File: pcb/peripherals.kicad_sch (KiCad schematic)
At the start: 1 part, among them U4 NRF24L01_Breakout

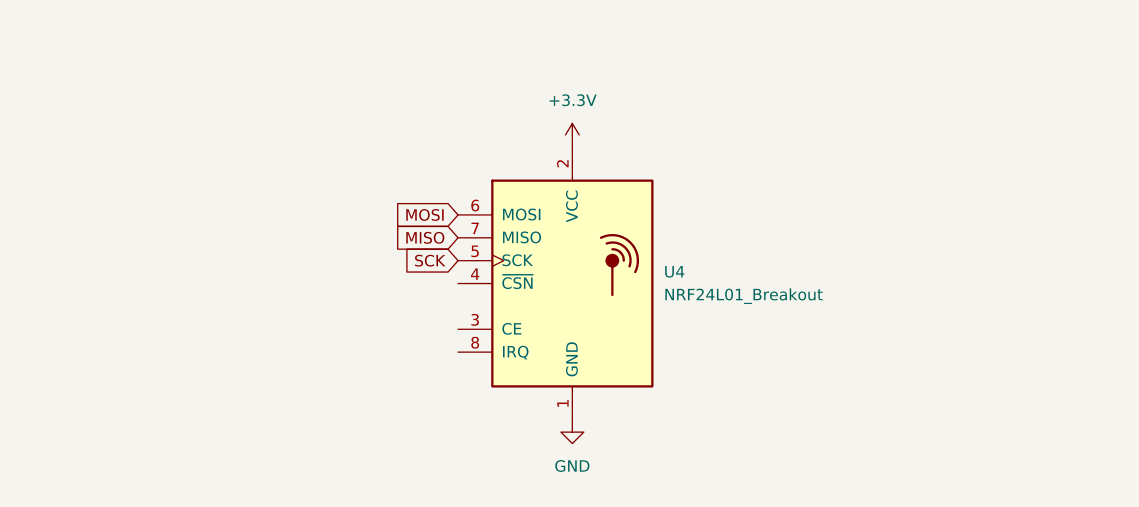
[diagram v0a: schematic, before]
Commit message: [pcb] motor controllers, label/group cleanup
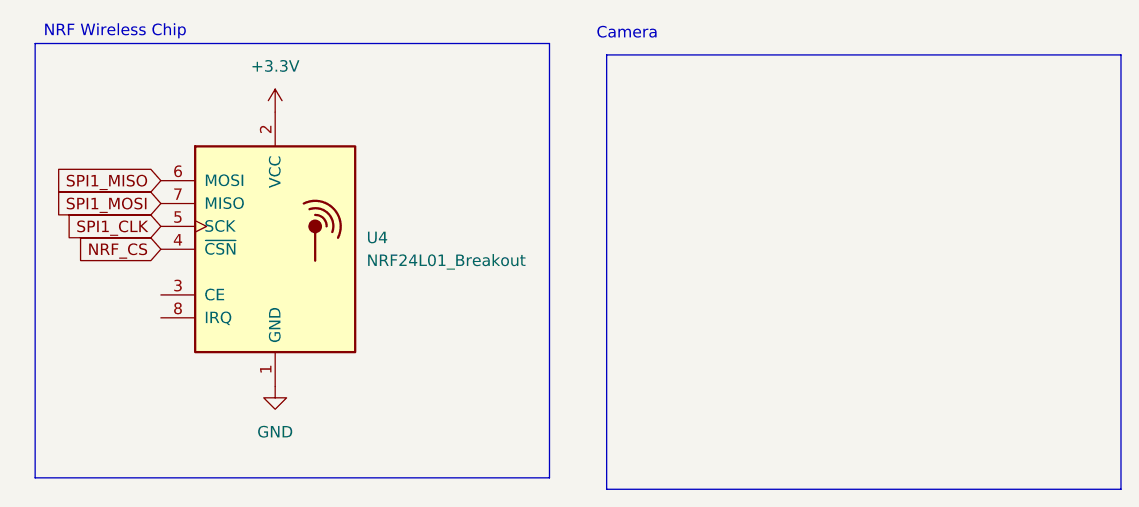
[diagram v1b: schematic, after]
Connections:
- net NRF_CS: now reaches U4.4 (~{CSN})
- net MISO renamed SPI1_MOSI
- net MOSI renamed SPI1_MISO
- net SCK renamed SPI1_CLK
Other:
- note added: "Camera"
- note added: "NRF Wireless Chip"
- moved on the sheet: U4
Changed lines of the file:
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@@
 	(generator_version "9.0")
 	(paper "A4")
-	(global_label "MOSI"
+	(rectangle
+		(start 82.55 17.78)
+		(end 139.7 66.04)
+		(stroke
+			(width 0)
+			(type default)
+		)
+		(fill
+			(type none)
+		)
+	)
+	(rectangle
+		(start 19.05 16.51)
+		(end 76.2 64.77)
+		(stroke
+			(width 0)
+			(type default)
+		)
+		(fill
+			(type none)
+		)
+	)
+	(text "Camera"
+		(exclude_from_sim no)
+		(at 84.836 15.494 0)
+		(effects
+			(font
+				(size 1.27 1.27)
+			)
+		)
+	)
+	(text "NRF Wireless Chip"
+		(exclude_from_sim no)
+		(at 27.94 15.24 0)
+		(effects
+			(font
+				(size 1.27 1.27)
+			)
+		)
+	)
+	(global_label "SPI1_CLK"
 		(shape input)
-		(at 66.04 35.56 180)
+		(at 33.02 36.83 180)
 		(fields_autoplaced yes)
 		(effects
@@
 		)
 		(property "Intersheetrefs" "${INTERSHEET_REFS}"
-			(at 58.4586 35.56 0)
+			(at 21.2053 36.83 0)
 			(effects
 				(font
@@
 		)
 	)
-	(global_label "MISO"
+	(global_label "SPI1_MISO"
 		(shape input)
-		(at 66.04 38.1 180)
+		(at 33.02 31.75 180)
 		(fields_autoplaced yes)
 		(effects
@@
 		)
 		(property "Intersheetrefs" "${INTERSHEET_REFS}"
-			(at 58.4586 38.1 0)
+			(at 20.1772 31.75 0)
 			(effects
 				(font
@@
 		)
 	)
-	(global_label "SCK"
+	(global_label "NRF_CS"
 		(shape input)
-		(at 66.04 40.64 180)
+		(at 33.02 39.37 180)
 		(fields_autoplaced yes)
 		(effects
@@
 		)
 		(property "Intersheetrefs" "${INTERSHEET_REFS}"
-			(at 59.3053 40.64 0)
+			(at 22.8986 39.37 0)
+			(effects
+				(font
+					(size 1.27 1.27)
+				)
+				(justify right)
+				(hide yes)
+			)
+		)
+	)
+	(global_label "SPI1_MOSI"
+		(shape input)
+		(at 33.02 34.29 180)
+		(fields_autoplaced yes)
+		(effects
+			(font
+				(size 1.27 1.27)
+			)
+			(justify right)
+		)
+		(property "Intersheetrefs" "${INTERSHEET_REFS}"
+			(at 20.1772 34.29 0)
 			(effects
 				(font
@@
 	(symbol
 		(lib_id "RF:NRF24L01_Breakout")
-		(at 78.74 43.18 0)
+		(at 45.72 39.37 0)
 		(unit 1)
 		(exclude_from_sim no)
@@
 		(fields_autoplaced yes)
 		(property "Reference" "U4"
-			(at 88.9 41.9099 0)
+			(at 55.88 38.0999 0)
 			(effects
 				(font
@@
 		)
 		(property "Value" "NRF24L01_Breakout"
-			(at 88.9 44.4499 0)
+			(at 55.88 40.6399 0)
 			(effects
 				(font
@@
 		)
 		(property "Footprint" "RF_Module:nRF24L01_Breakout"
-			(at 82.55 27.94 0)
+			(at 49.53 24.13 0)
 			(effects
 				(font
@@
 		)
 		(property "Datasheet" "http://www.nordicsemi.com/eng/content/download/2730/34105/file/nRF24L01_Product_Specification_v2_0.pdf"
-			(at 78.74 45.72 0)
+			(at 45.72 41.91 0)
 			(effects
 				(font
@@
 		)
 		(property "Description" "Ultra low power 2.4GHz RF Transceiver, Carrier PCB"
-			(at 78.74 43.18 0)
+			(at 45.72 39.37 0)
 			(effects
 				(font
@@
 	(symbol
 		(lib_id "power:+3.3V")
-		(at 78.74 27.94 0)
+		(at 45.72 24.13 0)
 		(unit 1)
 		(exclude_from_sim no)
@@
 		(fields_autoplaced yes)
 		(property "Reference" "#PWR022"
-			(at 78.74 31.75 0)
+			(at 45.72 27.94 0)
 			(effects
 				(font
@@
 		)
 		(property "Value" "+3.3V"
-			(at 78.74 22.86 0)
+			(at 45.72 19.05 0)
 			(effects
 				(font
@@
 		)
 		(property "Footprint" ""
-			(at 78.74 27.94 0)
+			(at 45.72 24.13 0)
 			(effects
 				(font
@@
 		)
 		(property "Datasheet" ""
-			(at 78.74 27.94 0)
+			(at 45.72 24.13 0)
 			(effects
 				(font
@@
 		)
 		(property "Description" "Power symbol creates a global label with name \"+3.3V\""
-			(at 78.74 27.94 0)
+			(at 45.72 24.13 0)
 			(effects
 				(font
@@
 	(symbol
 		(lib_id "power:GND")
-		(at 78.74 58.42 0)
+		(at 45.72 54.61 0)
 		(unit 1)
 		(exclude_from_sim no)
@@
 		(fields_autoplaced yes)
 		(property "Reference" "#PWR021"
-			(at 78.74 64.77 0)
+			(at 45.72 60.96 0)
 			(effects
 				(font
@@
 		)
 		(property "Value" "GND"
-			(at 78.74 63.5 0)
+			(at 45.72 59.69 0)
 			(effects
 				(font
@@
 		)
 		(property "Footprint" ""
-			(at 78.74 58.42 0)
+			(at 45.72 54.61 0)
 			(effects
 				(font
@@
 		)
 		(property "Datasheet" ""
-			(at 78.74 58.42 0)
+			(at 45.72 54.61 0)
 			(effects
 				(font
@@
 		)
 		(property "Description" "Power symbol creates a global label with name \"GND\" , ground"
-			(at 78.74 58.42 0)
-			(effects
-				(font
+			(at 45.72 54.61 0)
+			(effects
+				(font

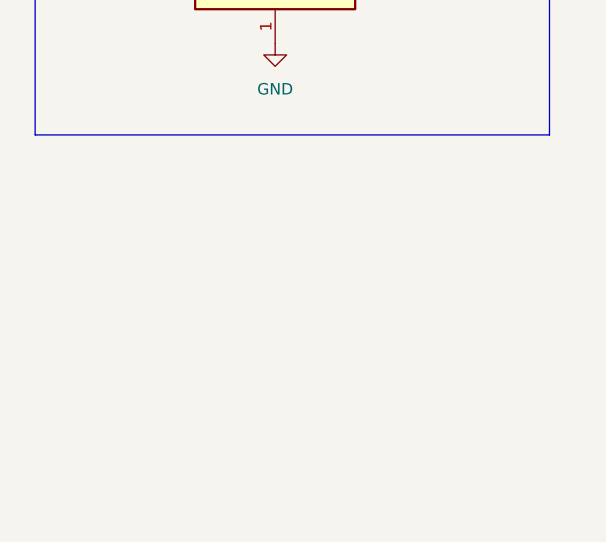
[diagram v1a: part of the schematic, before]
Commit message: [pcb] improve MCU analog power, battery voltage measurement, JTAG header
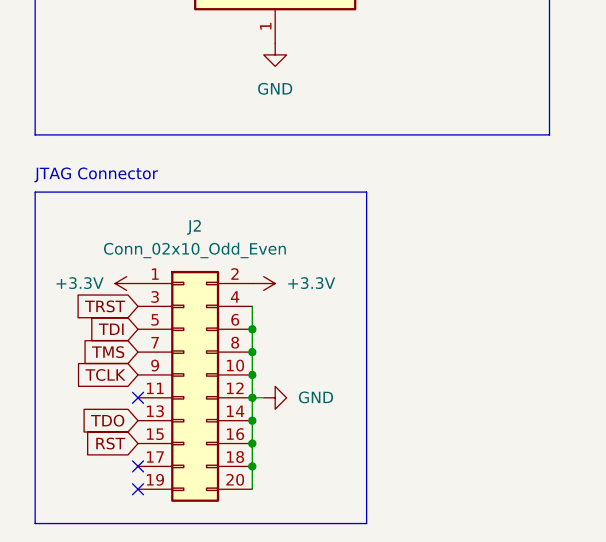
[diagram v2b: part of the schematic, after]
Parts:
- added J2: Conn_02x10_Odd_Even, Connector_PinHeader_2.54mm:PinHeader_2x10_P2.54mm_Vertical, symbol Connector_Generic:Conn_02x10_Odd_Even
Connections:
- net +3.3V: now also J2.1 (Pin_1), J2.2 (Pin_2)
- net GND: now also J2.10 (Pin_10), J2.12 (Pin_12), J2.14 (Pin_14), J2.16 (Pin_16), J2.18 (Pin_18), J2.20 (Pin_20), J2.4 (Pin_4), J2.6 (Pin_6), J2.8 (Pin_8)
- new net RST: J2.15 (Pin_15)
- new net TCLK: J2.9 (Pin_9)
- new net TDI: J2.5 (Pin_5)
- new net TDO: J2.13 (Pin_13)
- new net TMS: J2.7 (Pin_7)
- new net TRST: J2.3 (Pin_3)
- no-connect marks 0 -> 3
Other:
- note added: "JTAG Connector"

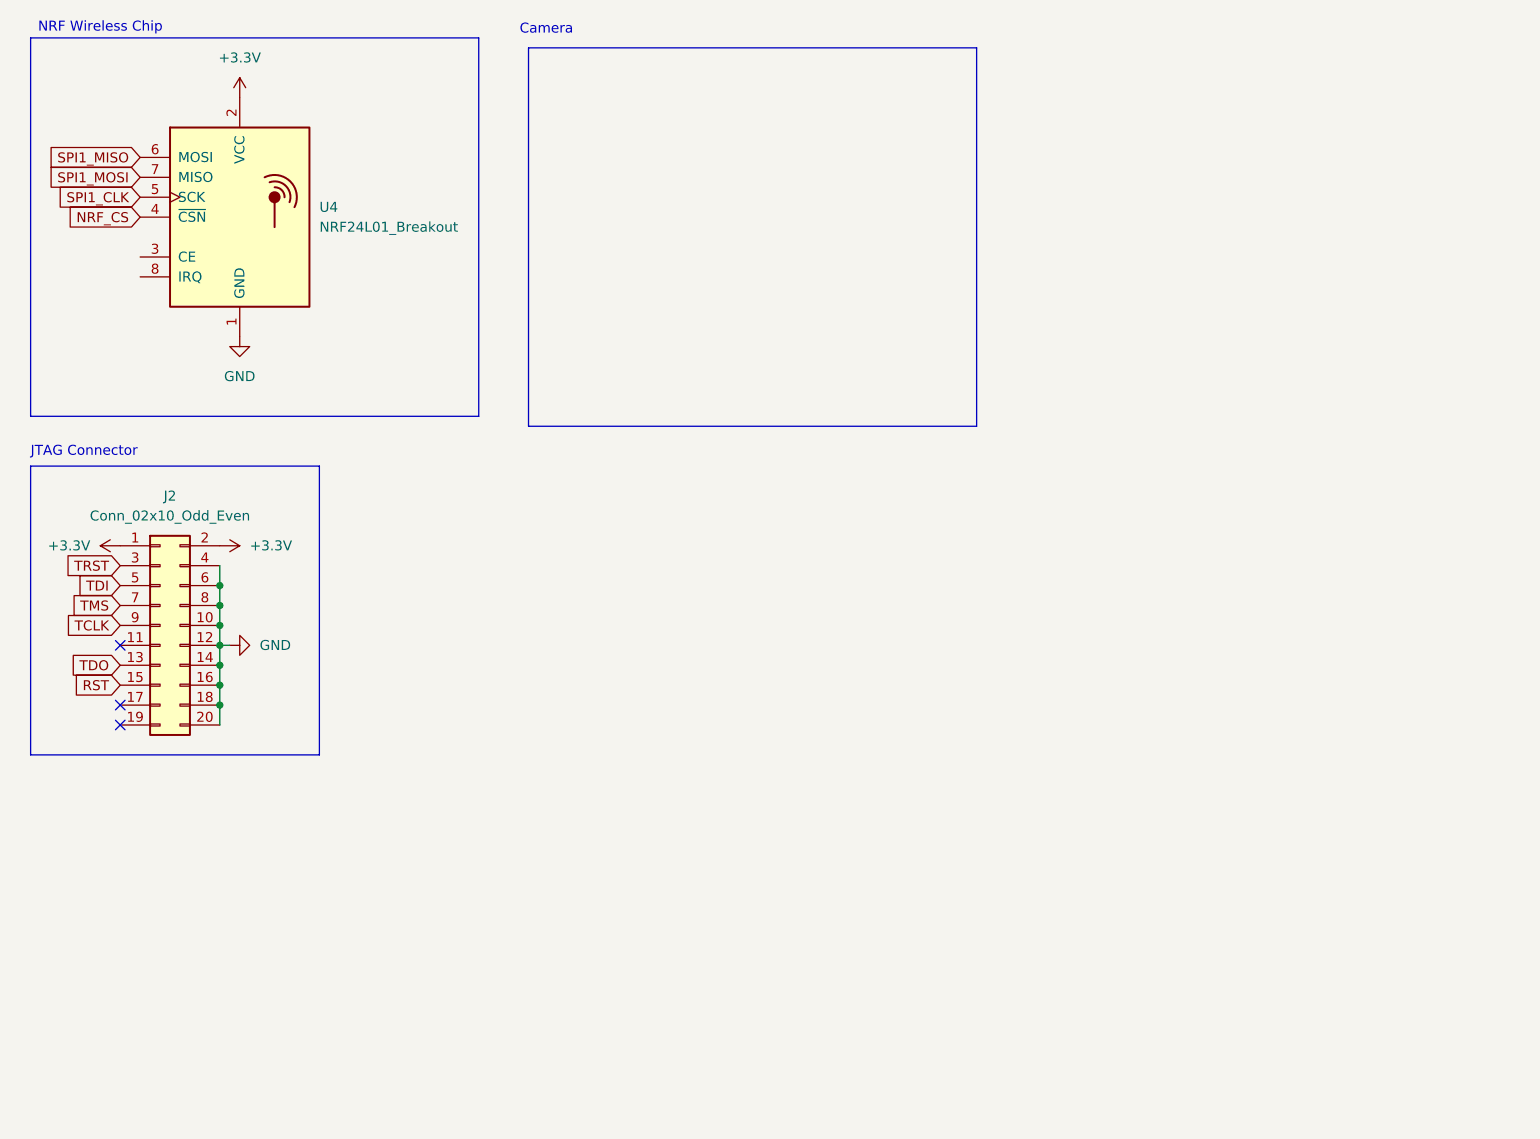
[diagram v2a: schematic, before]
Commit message: [pcb] gpio selection, camera, crystal
- Each motors is connected to a channel of TIM1
- The battery voltage divider is connected to ADC1
- The NRF24 is connected to SPI2
- Added OV5640 camera (FPC connector) + LDOs
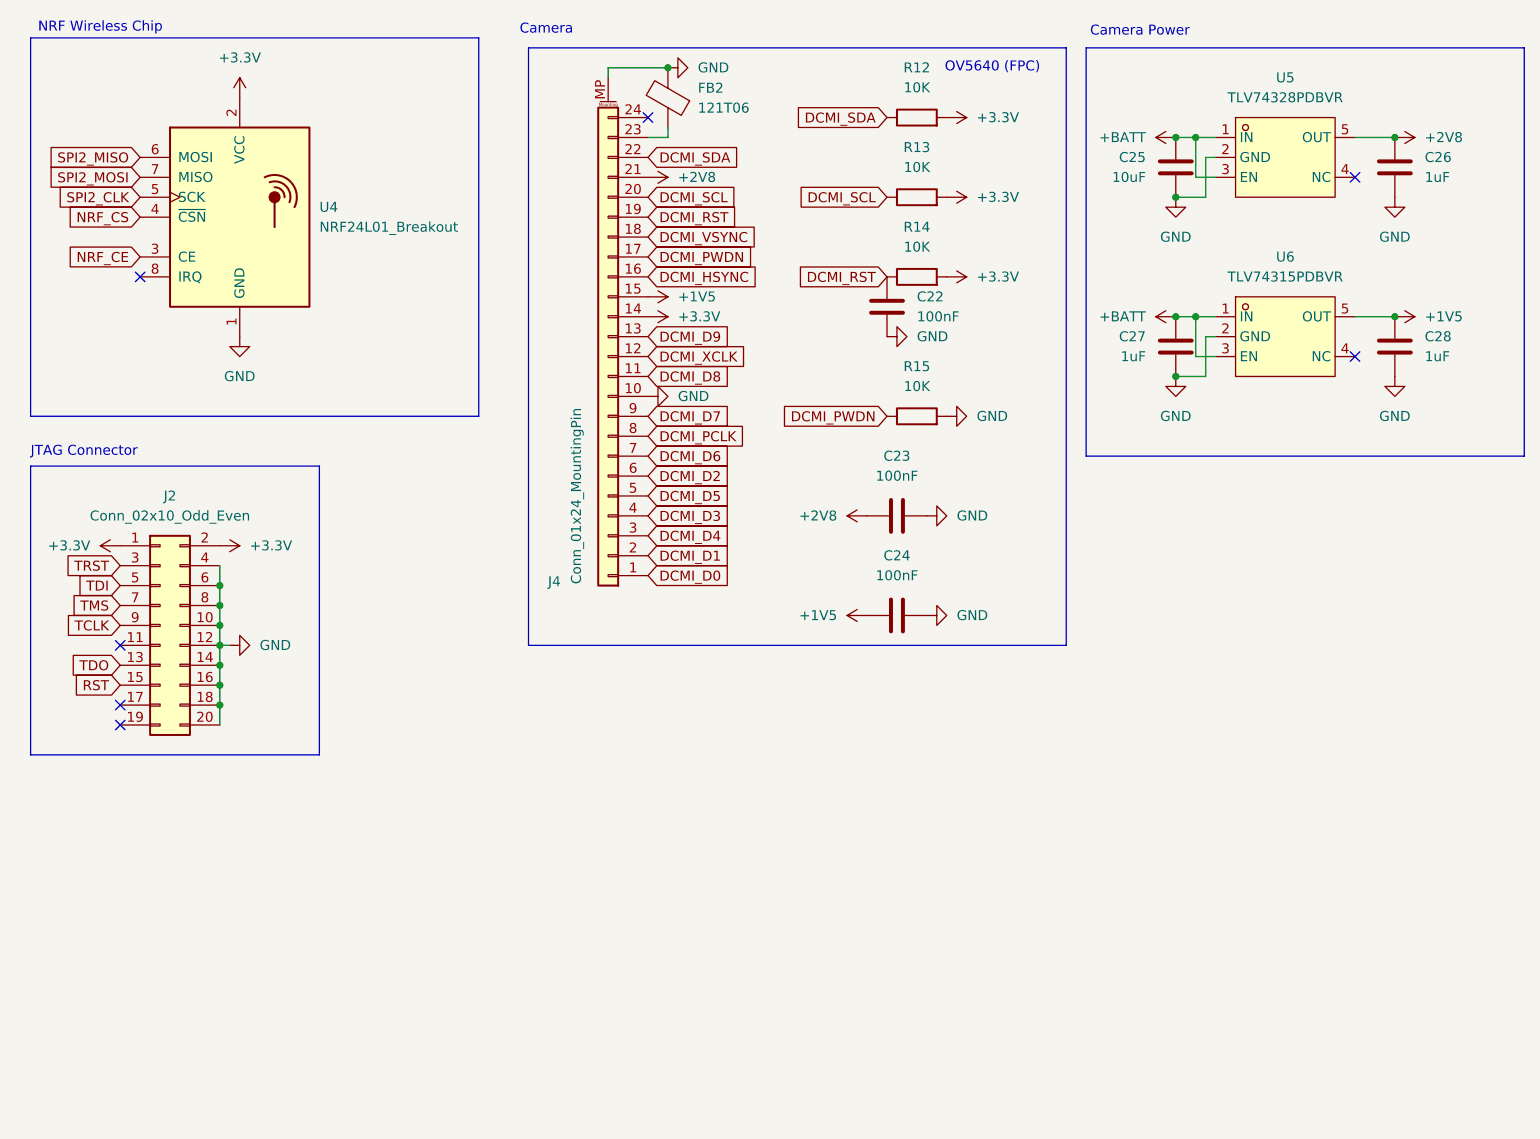
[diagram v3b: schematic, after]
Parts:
- added C22, C23, C24: 100nF, symbol Device:C
- added C25: 10uF, symbol Device:C
- added C26, C27, C28: 1uF, symbol Device:C
- added FB2: 121T06, symbol Device:FerriteBead
- added J4: Conn_01x24_MountingPin, symbol Connector_Generic_MountingPin:Conn_01x24_MountingPin
- added R12, R13, R14, R15: 10K, symbol Device:R
- added U5: TLV74328PDBVR, lcsc:SOT-23-5_L3.0-W1.7-P0.95-LS2.8-BL, symbol lcsc:TLV74328PDBVR
- added U6: TLV74315PDBVR, lcsc:SOT-23-5_L3.0-W1.7-P0.95-LS2.8-BL, symbol lcsc:TLV74328PDBVR
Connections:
- net +3.3V: now also J4.14 (Pin_14), R12.2, R13.2, R14.2
- net GND: now also C22.2, C23.2, C24.2, C25.2, C26.2, C27.2, C28.2, FB2.2, J4.10 (Pin_10), J4.MP (MountPin), R15.2, U5.2 (GND), U6.2 (GND)
- net NRF_CE: now reaches U4.3 (CE)
- net SPI1_CLK renamed SPI2_CLK
- net SPI1_MISO renamed SPI2_MISO
- net SPI1_MOSI renamed SPI2_MOSI
- new net: FB2.1, J4.23 (Pin_23)
- new net +1V5: C24.1, C28.1, J4.15 (Pin_15), U6.5 (OUT)
- new net +2V8: C23.1, C26.1, J4.21 (Pin_21), U5.5 (OUT)
- new net +BATT: C25.1, C27.1, U5.1 (IN), U5.3 (EN), U6.1 (IN), U6.3 (EN)
- new net DCMI_D0: J4.1 (Pin_1)
- new net DCMI_D1: J4.2 (Pin_2)
- new net DCMI_D2: J4.6 (Pin_6)
- new net DCMI_D3: J4.4 (Pin_4)
- new net DCMI_D4: J4.3 (Pin_3)
- new net DCMI_D5: J4.5 (Pin_5)
- new net DCMI_D6: J4.7 (Pin_7)
- new net DCMI_D7: J4.9 (Pin_9)
- new net DCMI_D8: J4.11 (Pin_11)
- new net DCMI_D9: J4.13 (Pin_13)
- new net DCMI_HSYNC: J4.16 (Pin_16)
- new net DCMI_PCLK: J4.8 (Pin_8)
- new net DCMI_PWDN: J4.17 (Pin_17), R15.1
- new net DCMI_RST: C22.1, J4.19 (Pin_19), R14.1
- new net DCMI_SCL: J4.20 (Pin_20), R13.1
- new net DCMI_SDA: J4.22 (Pin_22), R12.1
- new net DCMI_VSYNC: J4.18 (Pin_18)
- new net DCMI_XCLK: J4.12 (Pin_12)
- no-connect marks 3 -> 7
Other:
- note added: "Camera Power"
- note added: "OV5640 (FPC)"

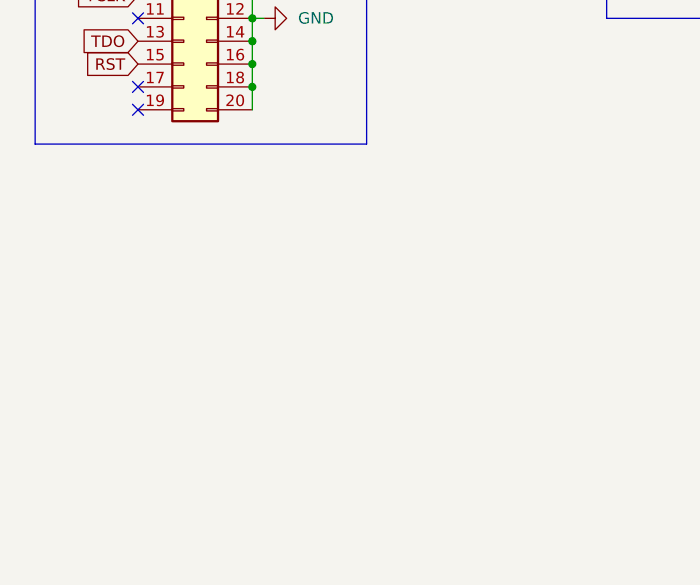
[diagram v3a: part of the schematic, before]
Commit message: [pcb] add imu
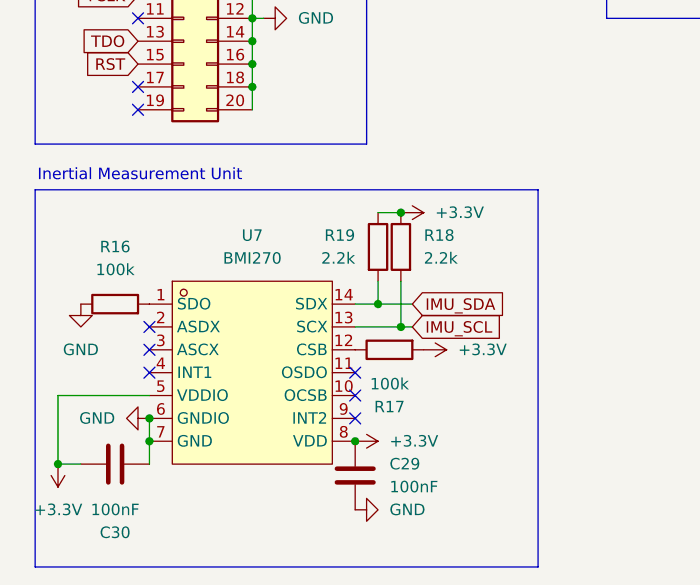
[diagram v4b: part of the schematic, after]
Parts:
- added C29, C30: 100nF, symbol Device:C
- added R16, R17: 100k, symbol Device:R
- added R18, R19: 2.2k, symbol Device:R
- added U7: BMI270, lcsc:LGA-14_L3.0-W2.5-P0.50-BR, symbol lcsc:BMI270
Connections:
- net +3.3V: now also C29.1, C30.1, R17.2, R18.1, R19.1, U7.5 (VDDIO), U7.8 (VDD)
- net GND: now also C29.2, C30.2, R16.1, U7.6 (GNDIO), U7.7 (GND)
- new net: R16.2, U7.1 (SDO)
- new net: R17.1, U7.12 (CSB)
- new net IMU_SCL: R18.2, U7.13 (SCX)
- new net IMU_SDA: R19.2, U7.14 (SDX)
- no-connect marks 7 -> 13
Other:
- note added: "Inertial Measurement Unit"

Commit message: [bom] pcb components and [pcb] assign footprints
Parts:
- C22: renamed from C25; footprint (none) -> Capacitor_SMD:C_0805_2012Metric_Pad1.18x1.45mm_HandSolder
- C23: renamed from C26; footprint (none) -> Capacitor_SMD:C_0805_2012Metric_Pad1.18x1.45mm_HandSolder
- C24: renamed from C22; footprint (none) -> Capacitor_SMD:C_0805_2012Metric_Pad1.18x1.45mm_HandSolder
- C25: renamed from C27; footprint (none) -> Capacitor_SMD:C_0805_2012Metric_Pad1.18x1.45mm_HandSolder
- C26: renamed from C28; footprint (none) -> Capacitor_SMD:C_0805_2012Metric_Pad1.18x1.45mm_HandSolder
- C27: renamed from C23; footprint (none) -> Capacitor_SMD:C_0805_2012Metric_Pad1.18x1.45mm_HandSolder
- C28: renamed from C24; footprint (none) -> Capacitor_SMD:C_0805_2012Metric_Pad1.18x1.45mm_HandSolder
- C29: renamed from C30; footprint (none) -> Capacitor_SMD:C_0805_2012Metric_Pad1.18x1.45mm_HandSolder
- C30: renamed from C29; footprint (none) -> Capacitor_SMD:C_0805_2012Metric_Pad1.18x1.45mm_HandSolder
- FB2: footprint (none) -> Inductor_SMD:L_0603_1608Metric_Pad1.05x0.95mm_HandSolder
- J2: renamed from J4; footprint (none) -> Connector_FFC-FPC:JUSHUO_AFA07-S24FCA-00_1x24-1MP_P1.0mm_Horizontal
- R12, R13, R14, R15: value 10K -> 10k; footprint (none) -> Resistor_SMD:R_0805_2012Metric_Pad1.20x1.40mm_HandSolder
- R16: renamed from R19; footprint (none) -> Resistor_SMD:R_0805_2012Metric_Pad1.20x1.40mm_HandSolder
- R17: renamed from R18; footprint (none) -> Resistor_SMD:R_0805_2012Metric_Pad1.20x1.40mm_HandSolder
- R18: renamed from R16; footprint (none) -> Resistor_SMD:R_0805_2012Metric_Pad1.20x1.40mm_HandSolder
- R19: renamed from R17; footprint (none) -> Resistor_SMD:R_0805_2012Metric_Pad1.20x1.40mm_HandSolder
- U4: renamed from U5; footprint lcsc:SOT-23-5_L3.0-W1.7-P0.95-LS2.8-BL -> Package_TO_SOT_SMD:SOT-23-5_HandSoldering
- U6: footprint lcsc:SOT-23-5_L3.0-W1.7-P0.95-LS2.8-BL -> Package_TO_SOT_SMD:SOT-23-5_HandSoldering
- renumbered J2 to J3, U4 to U5
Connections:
- net SPI2_MISO: now also U5.7 (MISO); no longer U5.6 (MOSI)
- net SPI2_MOSI: now also U5.6 (MOSI); no longer U5.7 (MISO)

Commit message: [pcb] initial layout and power routing
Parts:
- U5: footprint RF_Module:nRF24L01_Breakout -> lcsc:nRF24L01_SMD_Breakout
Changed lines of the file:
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@@
 			)
 		)
-		(property "Footprint" "RF_Module:nRF24L01_Breakout"
+		(property "Footprint" "lcsc:nRF24L01_SMD_Breakout"
 			(at 49.53 24.13 0)
 			(effects
